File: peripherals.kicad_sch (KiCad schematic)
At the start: 7 parts, among them J10 VSYS, J11 LSOUT1, J12 LSOUT2, J6 GPS, J7 LoRa, J8 Sensors, J9 RCC

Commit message: assigned footprint and created PCB file
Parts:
- J10, J11, J12, J6, J7: footprint (none) -> Connector_PinHeader_2.54mm:PinHeader_1x02_P2.54mm_Vertical
- J8: footprint (none) -> Connector_PinHeader_2.54mm:PinHeader_1x06_P2.54mm_Vertical
- J9: footprint (none) -> Connector_PinHeader_2.54mm:PinHeader_1x01_P2.54mm_Vertical
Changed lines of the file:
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@@
 			)
 		)
-		(property "Footprint" ""
+		(property "Footprint" "Connector_PinHeader_2.54mm:PinHeader_1x02_P2.54mm_Vertical"
 			(at 116.84 83.82 0)
 			(hide yes)
@@
 			)
 		)
-		(property "Footprint" ""
+		(property "Footprint" "Connector_PinHeader_2.54mm:PinHeader_1x02_P2.54mm_Vertical"
 			(at 116.84 68.58 0)
 			(hide yes)
@@
 			)
 		)
-		(property "Footprint" ""
+		(property "Footprint" "Connector_PinHeader_2.54mm:PinHeader_1x02_P2.54mm_Vertical"
 			(at 165.1 97.79 0)
 			(hide yes)
@@
 			)
 		)
-		(property "Footprint" ""
+		(property "Footprint" "Connector_PinHeader_2.54mm:PinHeader_1x01_P2.54mm_Vertical"
 			(at 116.84 130.81 0)
 			(hide yes)
@@
 			)
 		)
-		(property "Footprint" ""
+		(property "Footprint" "Connector_PinHeader_2.54mm:PinHeader_1x02_P2.54mm_Vertical"
 			(at 165.1 111.76 0)
 			(hide yes)
@@
 			)
 		)
-		(property "Footprint" ""
+		(property "Footprint" "Connector_PinHeader_2.54mm:PinHeader_1x06_P2.54mm_Vertical"
 			(at 116.84 107.95 0)
 			(hide yes)
@@
 			)
 		)
-		(property "Footprint" ""
+		(property "Footprint" "Connector_PinHeader_2.54mm:PinHeader_1x02_P2.54mm_Vertical"
 			(at 165.1 82.55 0)
 			(hide yes)

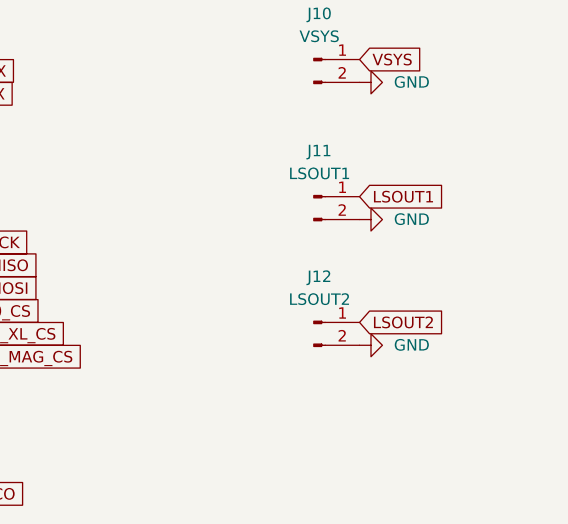
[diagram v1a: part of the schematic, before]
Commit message: migrated display power with lora
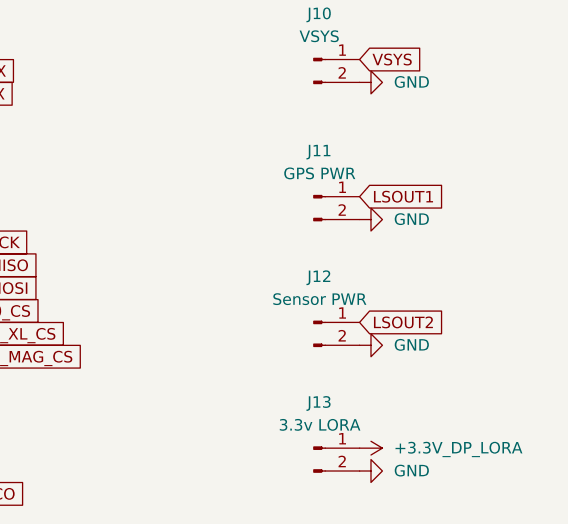
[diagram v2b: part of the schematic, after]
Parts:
- added J13: 3.3v LORA, Connector_PinHeader_2.54mm:PinHeader_1x02_P2.54mm_Vertical, symbol Connector:Conn_01x02_Pin
- J11: value LSOUT1 -> GPS PWR
- J12: value LSOUT2 -> Sensor PWR
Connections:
- net GND: now also J13.2 (Pin_2)
- new net +3.3V_DP_LORA: J13.1 (Pin_1)
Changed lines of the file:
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@@
 			)
 		)
-		(property "Value" "LSOUT1"
+		(property "Value" "GPS PWR"
 			(at 165.735 95.25 0)
 			(show_name no)
@@
 				(path "/3b4a40c0-7c9d-4ce8-93f8-431f93ad7804"
 					(reference "J11")
+					(unit 1)
+				)
+			)
+		)
+	)
+	(symbol
+		(lib_id "Connector:Conn_01x02_Pin")
+		(at 165.1 125.73 0)
+		(unit 1)
+		(body_style 1)
+		(exclude_from_sim no)
+		(in_bom yes)
+		(on_board yes)
+		(in_pos_files yes)
+		(dnp no)
+		(fields_autoplaced yes)
+		(property "Reference" "J13"
+			(at 165.735 120.65 0)
+			(show_name no)
+			(do_not_autoplace no)
+			(effects
+				(font
+					(size 1.27 1.27)
+				)
+			)
+		)
+		(property "Value" "3.3v LORA"
+			(at 165.735 123.19 0)
+			(show_name no)
+			(do_not_autoplace no)
+			(effects
+				(font
+					(size 1.27 1.27)
+				)
+			)
+		)
+		(property "Footprint" "Connector_PinHeader_2.54mm:PinHeader_1x02_P2.54mm_Vertical"
+			(at 165.1 125.73 0)
+			(hide yes)
+			(show_name no)
+			(do_not_autoplace no)
+			(effects
+				(font
+					(size 1.27 1.27)
+				)
+			)
+		)
+		(property "Datasheet" ""
+			(at 165.1 125.73 0)
+			(hide yes)
+			(show_name no)
+			(do_not_autoplace no)
+			(effects
+				(font
+					(size 1.27 1.27)
+				)
+			)
+		)
+		(property "Description" "Generic connector, single row, 01x02, script generated"
+			(at 165.1 125.73 0)
+			(hide yes)
+			(show_name no)
+			(do_not_autoplace no)
+			(effects
+				(font
+					(size 1.27 1.27)
+				)
+			)
+		)
+		(pin "1"
+		)
+		(pin "2"
+		)
+		(instances
+			(project "TheSummitProject"
+				(path "/3b4a40c0-7c9d-4ce8-93f8-431f93ad7804"
+					(reference "J13")
+					(unit 1)
+				)
+			)
+		)
+	)
+	(symbol
+		(lib_id "power:+3.3VP")
+		(at 170.18 125.73 270)
+		(unit 1)
+		(body_style 1)
+		(exclude_from_sim no)
+		(in_bom yes)
+		(on_board yes)
+		(in_pos_files yes)
+		(dnp no)
+		(fields_autoplaced yes)
+		(property "Reference" "#PWR016"
+			(at 168.91 129.54 0)
+			(hide yes)
+			(show_name no)
+			(do_not_autoplace no)
+			(effects
+				(font
+					(size 1.27 1.27)
+				)
+			)
+		)
+		(property "Value" "+3.3V_DP_LORA"
+			(at 173.99 125.7299 90)
+			(show_name no)
+			(do_not_autoplace no)
+			(effects
+				(font
+					(size 1.27 1.27)
+				)
+				(justify left)
+			)
+		)
+		(property "Footprint" ""
+			(at 170.18 125.73 0)
+			(hide yes)
+			(show_name no)
+			(do_not_autoplace no)
+			(effects
+				(font
+					(size 1.27 1.27)
+				)
+			)
+		)
+		(property "Datasheet" ""
+			(at 170.18 125.73 0)
+			(hide yes)
+			(show_name no)
+			(do_not_autoplace no)
+			(effects
+				(font
+					(size 1.27 1.27)
+				)
+			)
+		)
+		(property "Description" "Power symbol creates a global label with name \"+3.3VP\""
+			(at 170.18 125.73 0)
+			(hide yes)
+			(show_name no)
+			(do_not_autoplace no)
+			(effects
+				(font
+					(size 1.27 1.27)
+				)
+			)
+		)
+		(pin "1"
+		)
+		(instances
+			(project "TheSummitProject"
+				(path "/3b4a40c0-7c9d-4ce8-93f8-431f93ad7804"
+					(reference "#PWR016")
 					(unit 1)
 				)
@@
 			)
 		)
-		(property "Value" "LSOUT2"
+		(property "Value" "Sensor PWR"
 			(at 165.735 109.22 0)
 			(show_name no)
@@
 					(unit 1)
 				)
+			)
+		)
+	)
+	(symbol
+		(lib_id "power:GND")
+		(at 170.18 128.27 90)
+		(unit 1)
+		(body_style 1)
+		(exclude_from_sim no)
+		(in_bom yes)
+		(on_board yes)
+		(in_pos_files yes)
+		(dnp no)
+		(fields_autoplaced yes)
+		(property "Reference" "#PWR069"
+			(at 176.53 128.27 0)
+			(hide yes)
+			(show_name no)
+			(do_not_autoplace no)
+			(effects
+				(font
+					(size 1.27 1.27)
+				)
+			)
+		)
+		(property "Value" "GND"
+			(at 173.99 128.2699 90)
+			(show_name no)
+			(do_not_autoplace no)
+			(effects
+				(font
+					(size 1.27 1.27)
+				)
+				(justify right)
+			)
+		)
+		(property "Footprint" ""
+			(at 170.18 128.27 0)
+			(hide yes)
+			(show_name no)
+			(do_not_autoplace no)
+			(effects
+				(font
+					(size 1.27 1.27)
+				)
+			)
+		)
+		(property "Datasheet" ""
+			(at 170.18 128.27 0)
+			(hide yes)
+			(show_name no)
+			(do_not_autoplace no)
+			(effects
+				(font
+					(size 1.27 1.27)
+				)
+			)
+		)
+		(property "Description" "Power symbol creates a global label with name \"GND\" , ground"
+			(at 170.18 128.27 0)
+			(hide yes)
+			(show_name no)
+			(do_not_autoplace no)
+			(effects
+				(font
+					(size 1.27 1.27)
+				)
+			)
+		)
+		(pin "1"
+		)
+		(instances
+			(project "TheSummitProject"
+				(path "/3b4a40c0-7c9d-4ce8-93f8-431f93ad7804"
+					(reference "#PWR069")
+					(unit 1)
+				)

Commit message: Updated footprints for RCC_MCO to test point
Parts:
- J9: footprint Connector_PinHeader_2.54mm:PinHeader_1x01_P2.54mm_Vertical -> TestPoint:TestPoint_Pad_D1.5mm
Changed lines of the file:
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@@
 			)
 		)
-		(property "Footprint" "Connector_PinHeader_2.54mm:PinHeader_1x01_P2.54mm_Vertical"
+		(property "Footprint" "TestPoint:TestPoint_Pad_D1.5mm"
 			(at 116.84 130.81 0)
 			(hide yes)

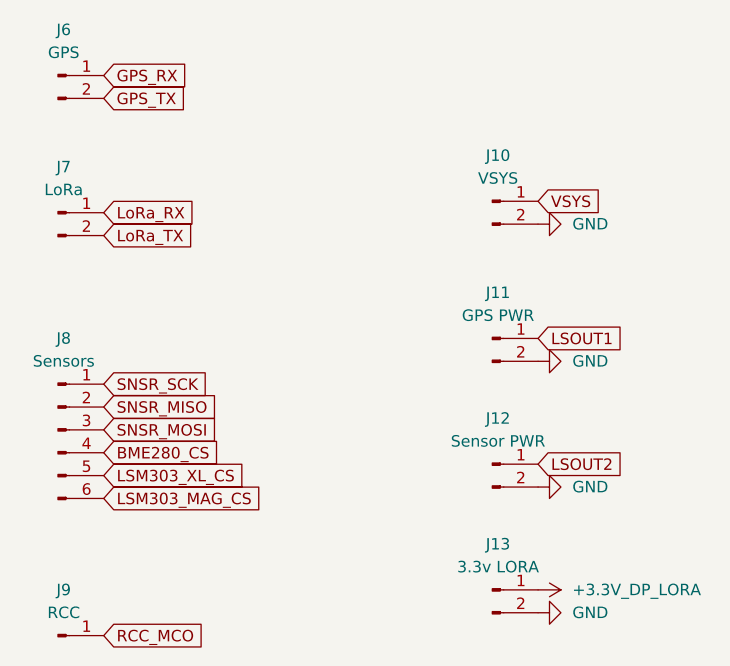
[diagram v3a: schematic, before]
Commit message: Changed pcb to 4 layers and completed 50% traces
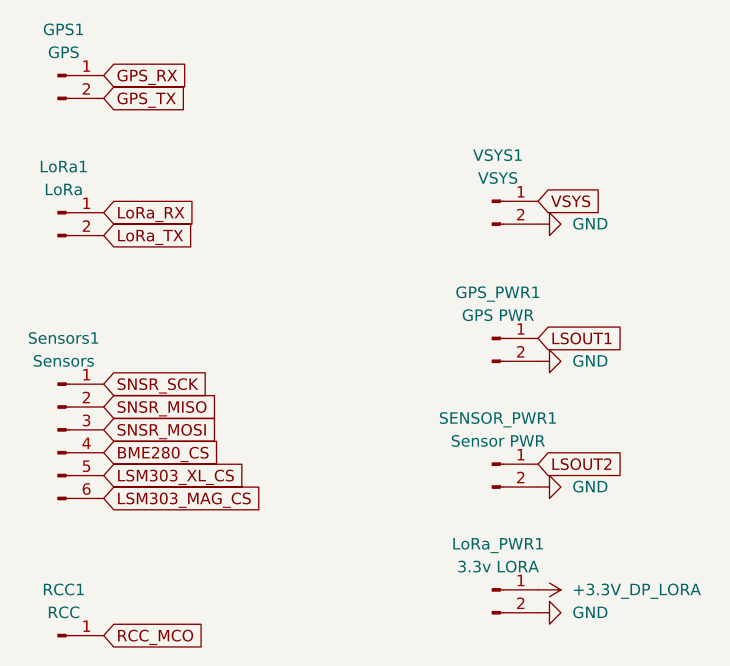
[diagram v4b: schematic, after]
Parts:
- renumbered J6 to GPS1, J11 to GPS_PWR1, J7 to LoRa1, J13 to LoRa_PWR1, J9 to RCC1, J12 to SENSOR_PWR1, J8 to Sensors1, J10 to VSYS1
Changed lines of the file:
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@@
 		(dnp no)
 		(fields_autoplaced yes)
-		(property "Reference" "J7"
+		(property "Reference" "LoRa1"
 			(at 117.475 78.74 0)
 			(show_name no)
@@
 			(project "TheSummitProject"
 				(path "/3b4a40c0-7c9d-4ce8-93f8-431f93ad7804"
-					(reference "J7")
+					(reference "LoRa1")
 					(unit 1)
 				)
@@
 		(dnp no)
 		(fields_autoplaced yes)
-		(property "Reference" "J6"
+		(property "Reference" "GPS1"
 			(at 117.475 63.5 0)
 			(show_name no)
@@
 			(project "TheSummitProject"
 				(path "/3b4a40c0-7c9d-4ce8-93f8-431f93ad7804"
-					(reference "J6")
+					(reference "GPS1")
 					(unit 1)
 				)
@@
 		(dnp no)
 		(fields_autoplaced yes)
-		(property "Reference" "J11"
+		(property "Reference" "GPS_PWR1"
 			(at 165.735 92.71 0)
 			(show_name no)
@@
 			(project "TheSummitProject"
 				(path "/3b4a40c0-7c9d-4ce8-93f8-431f93ad7804"
-					(reference "J11")
+					(reference "GPS_PWR1")
 					(unit 1)
 				)
@@
 		(dnp no)
 		(fields_autoplaced yes)
-		(property "Reference" "J13"
+		(property "Reference" "LoRa_PWR1"
 			(at 165.735 120.65 0)
 			(show_name no)
@@
 			(project "TheSummitProject"
 				(path "/3b4a40c0-7c9d-4ce8-93f8-431f93ad7804"
-					(reference "J13")
+					(reference "LoRa_PWR1")
 					(unit 1)
 				)
@@
 		(dnp no)
 		(fields_autoplaced yes)
-		(property "Reference" "J9"
+		(property "Reference" "RCC1"
 			(at 117.475 125.73 0)
 			(show_name no)
@@
 			(project "TheSummitProject"
 				(path "/3b4a40c0-7c9d-4ce8-93f8-431f93ad7804"
-					(reference "J9")
+					(reference "RCC1")
 					(unit 1)
 				)
@@
 		(dnp no)
 		(fields_autoplaced yes)
-		(property "Reference" "J12"
+		(property "Reference" "SENSOR_PWR1"
 			(at 165.735 106.68 0)
 			(show_name no)
@@
 			(project "TheSummitProject"
 				(path "/3b4a40c0-7c9d-4ce8-93f8-431f93ad7804"
-					(reference "J12")
+					(reference "SENSOR_PWR1")
 					(unit 1)
 				)
@@
 		(dnp no)
 		(fields_autoplaced yes)
-		(property "Reference" "J8"
+		(property "Reference" "Sensors1"
 			(at 117.475 97.79 0)
 			(show_name no)
@@
 			(project "TheSummitProject"
 				(path "/3b4a40c0-7c9d-4ce8-93f8-431f93ad7804"
-					(reference "J8")
+					(reference "Sensors1")
 					(unit 1)
 				)
@@
 		(dnp no)
 		(fields_autoplaced yes)
-		(property "Reference" "J10"
+		(property "Reference" "VSYS1"
 			(at 165.735 77.47 0)
 			(show_name no)
@@
 			(project "TheSummitProject"
 				(path "/3b4a40c0-7c9d-4ce8-93f8-431f93ad7804"
-					(reference "J10")
-					(unit 1)
-				)
+					(reference "VSYS1")
+					(unit 1)
+				)

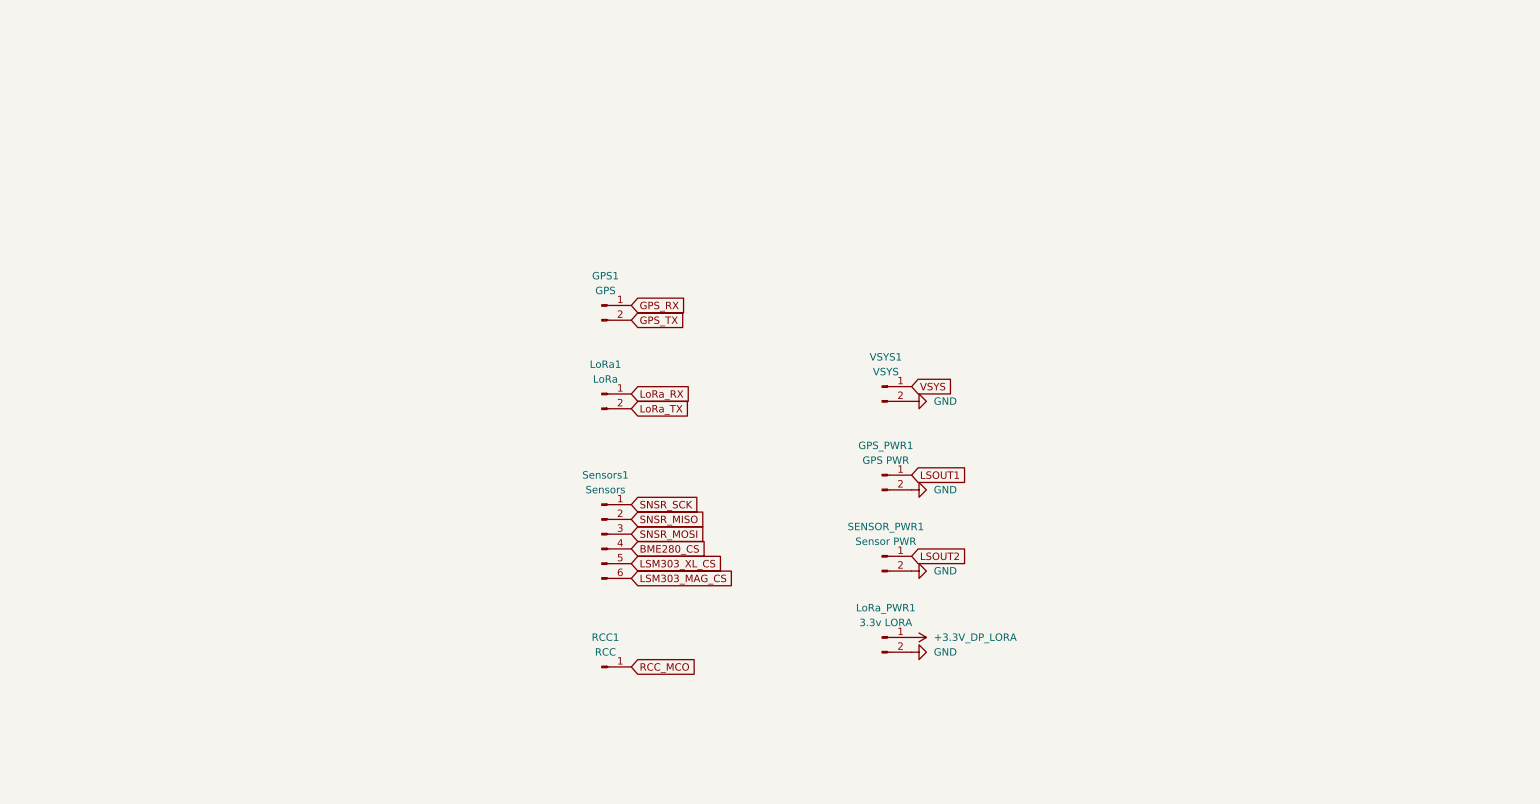
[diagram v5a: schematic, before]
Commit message: Updated with new power rails, added sensors and gps symbol
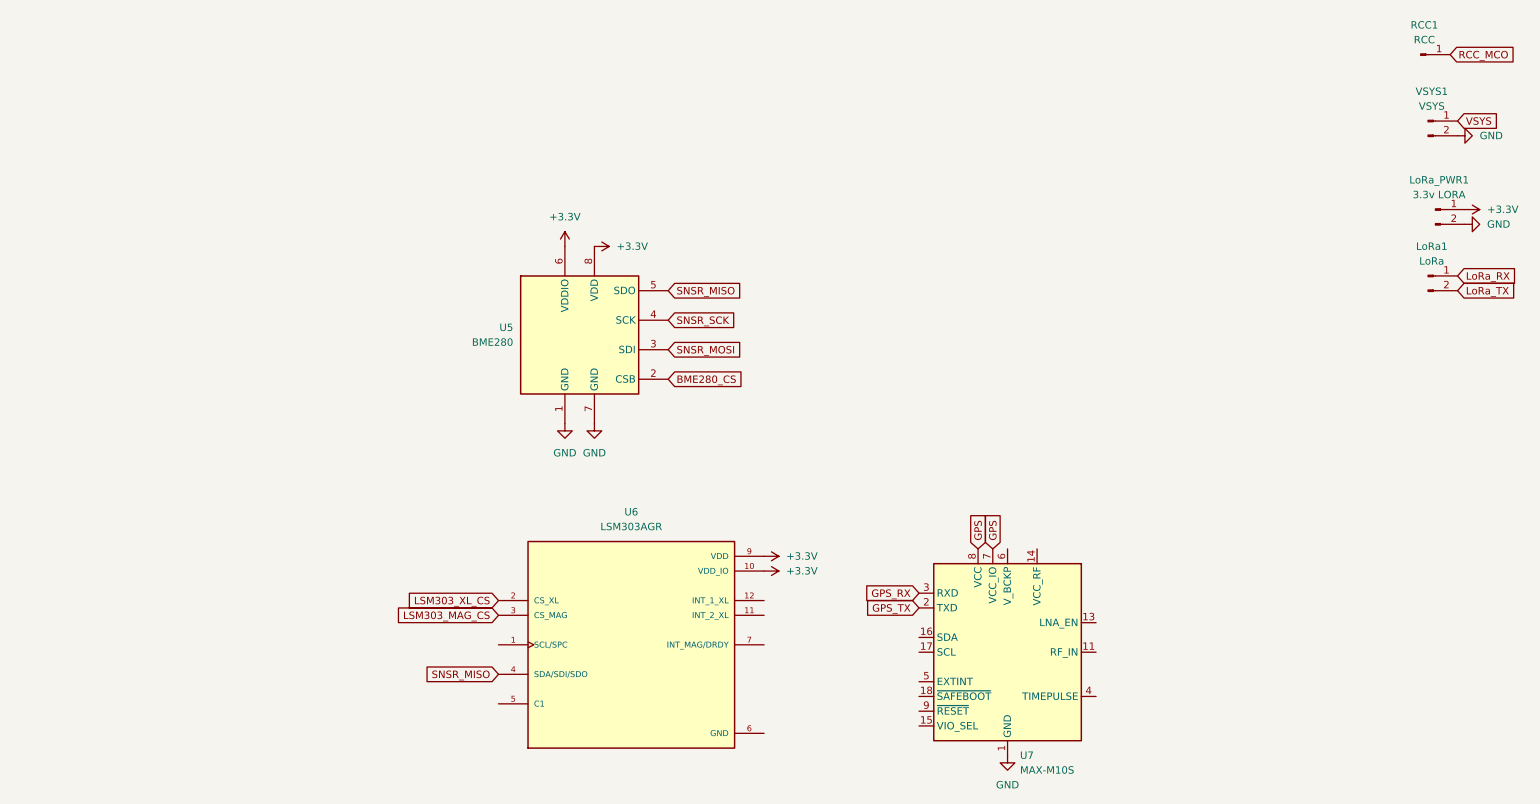
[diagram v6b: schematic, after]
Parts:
- removed GPS1: GPS, Connector_PinHeader_2.54mm:PinHeader_1x02_P2.54mm_Vertical, symbol Connector:Conn_01x02_Pin
- removed GPS_PWR1: GPS PWR, Connector_PinHeader_2.54mm:PinHeader_1x02_P2.54mm_Vertical, symbol Connector:Conn_01x02_Pin
- removed SENSOR_PWR1: Sensor PWR, Connector_PinHeader_2.54mm:PinHeader_1x02_P2.54mm_Vertical, symbol Connector:Conn_01x02_Pin
- removed Sensors1: Sensors, Connector_PinHeader_2.54mm:PinHeader_1x06_P2.54mm_Vertical, symbol Connector:Conn_01x06_Pin
- added U5: BME280, Package_LGA:Bosch_LGA-8_2.5x2.5mm_P0.65mm_ClockwisePinNumbering, symbol Sensor:BME280
- added U6: LSM303AGR, LSM303AGR:PQFN50P200X200X100-12N, symbol TheSummitProject:LSM303AGR
- added U7: MAX-M10S, RF_GPS:ublox_MAX, symbol RF_GPS:MAX-M10S
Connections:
- net BME280_CS: now also U5.2 (CSB)
- net GND: now also U5.1 (GND), U5.7 (GND), U6.6 (GND), U6.8 (GND), U7.1 (GND), U7.10 (GND), U7.12 (GND)
- net GPS_RX: now also U7.3 (RXD)
- net GPS_TX: now also U7.2 (TXD)
- net LSM303_MAG_CS: now also U6.3 (CS_MAG)
- net LSM303_XL_CS: now also U6.2 (CS_XL)
- net SNSR_MISO: now also U5.5 (SDO), U6.4 (SDA/SDI/SDO)
- net SNSR_MOSI: now also U5.3 (SDI)
- net SNSR_SCK: now also U5.4 (SCK)
- net +3.3V_DP_LORA renamed +3.3V
- net +3.3V: now also U5.6 (VDDIO), U5.8 (VDD), U6.10 (VDD_IO), U6.9 (VDD)
- new net GPS: U7.7 (VCC_IO), U7.8 (VCC)
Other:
- moved on the sheet: LoRa1, LoRa_PWR1, RCC1, VSYS1

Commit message: UPDATE U567
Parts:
- added C34: 220nf, symbol Device:C
- added C35, C36: 100nf, symbol Device:C
- added C37, C38: 100NF, symbol Device:C
- added J2: GPS_ANT, symbol Connector:Conn_Coaxial
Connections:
- net +3.3V: now also C35.2, C36.1, C37.2, C38.1
- net GND: now also C34.1, C35.1, C36.2, C37.1, C38.2, J2.2 (Ext)
- net SNSR_MISO: no longer U6.4 (SDA/SDI/SDO)
- net SNSR_MOSI: now also U6.4 (SDA/SDI/SDO)
- net SNSR_SCK: now also U6.1 (SCL/SPC)
- net at U6.5 (C1): now also C34.2
- net at U7.11 (RF_IN): now also J2.1 (In)
- no-connect marks 0 -> 13
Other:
- note added: "BME280"
- note added: "CAN DO A FALLING DETECT LATER"
- note added: "LSM303AGR"
- moved on the sheet: U5, U6, U7
